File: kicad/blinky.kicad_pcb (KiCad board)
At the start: 2 copper layers, 40 x 39.9 mm, 18 parts, among them J2 Val**, Q1 MMBT2222, Q2 MMBT2222, Q3 MMBT2222, Q4 MMBT2222

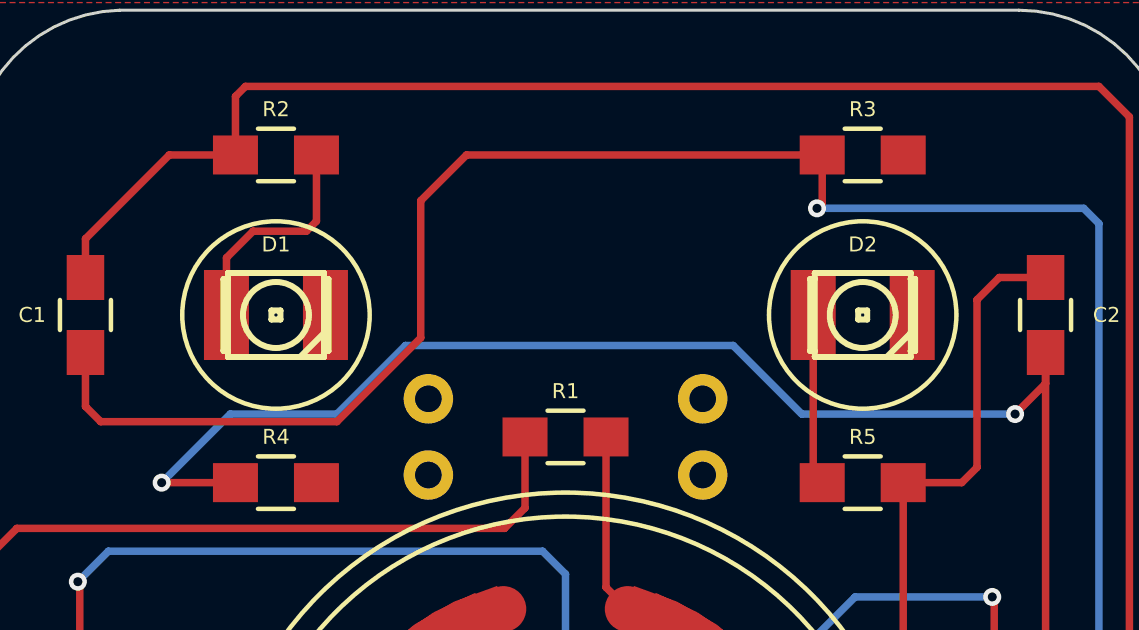
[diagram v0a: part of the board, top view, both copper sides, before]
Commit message: switched to 1206 LEDs
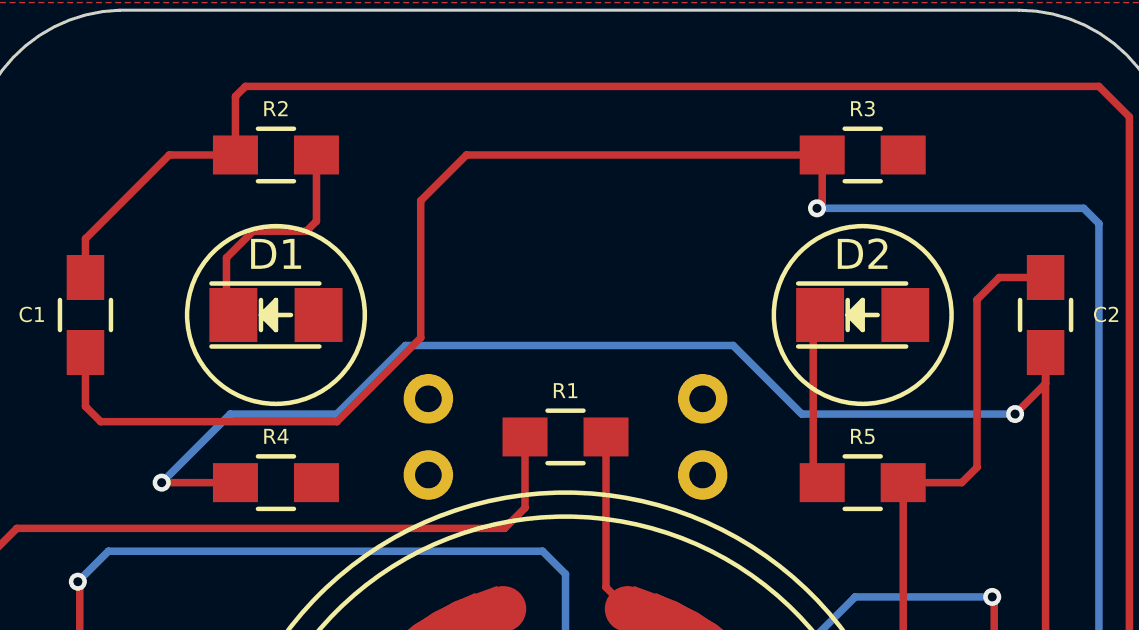
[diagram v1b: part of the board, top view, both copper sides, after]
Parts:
- D1, D2: footprint bb:MADW__PLCC2-3528 -> bb:LED-1206

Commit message: updated
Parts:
- Q1, Q2, Q3, Q4: footprint bb:SOT-23 -> bb:SOT-23_Handsoldering
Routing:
- net Net-(Q1-Pad1): track 88.4 -> 90.3 mm
- net Net-(C1-Pad1): track 77.4 -> 78.8 mm
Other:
- board text added: "blinky badge 1.1"
- board text removed: "blinky badge 1.0"
